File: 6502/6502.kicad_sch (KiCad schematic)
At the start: 34 parts, among them SW1 SW_Push, SW2 SW_Push, U1 74LS08, U10 NHD-0420H1Z, U12 65C02S, U2 ATF22V10C, U3 74LS154, U4 AS6C4008-55PCN, U5 28C256, U7 6522, U8 6522, X1 ACO-4MHz

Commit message: pcb almost done
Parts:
- C6: renamed from C15; footprint Capacitor_THT:C_Radial_D8.0mm_H7.0mm_P3.50mm -> Capacitor_THT:C_Radial_D10.0mm_H20.0mm_P5.00mm
- renumbered C8 to C10, C9 to C11, C6 to C7, C16 to C8, C7 to C9, R7 to R1, R5 to R2, R2 to R3, R8 to R5, R1 to R6, R9 to R7, R6 to R8, R3 to R9, SW2 to SW1, SW1 to SW2, U3 to U2, U5 to U3, U2 to U4, U12 to U5, U4 to U6, U10 to U9
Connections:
- net EXT_IN2: no longer U2.18 (E0), U4.3 (I1), U5.25 (A15)
- new net a15: U2.18 (E0), U4.3 (I1), U5.25 (A15)

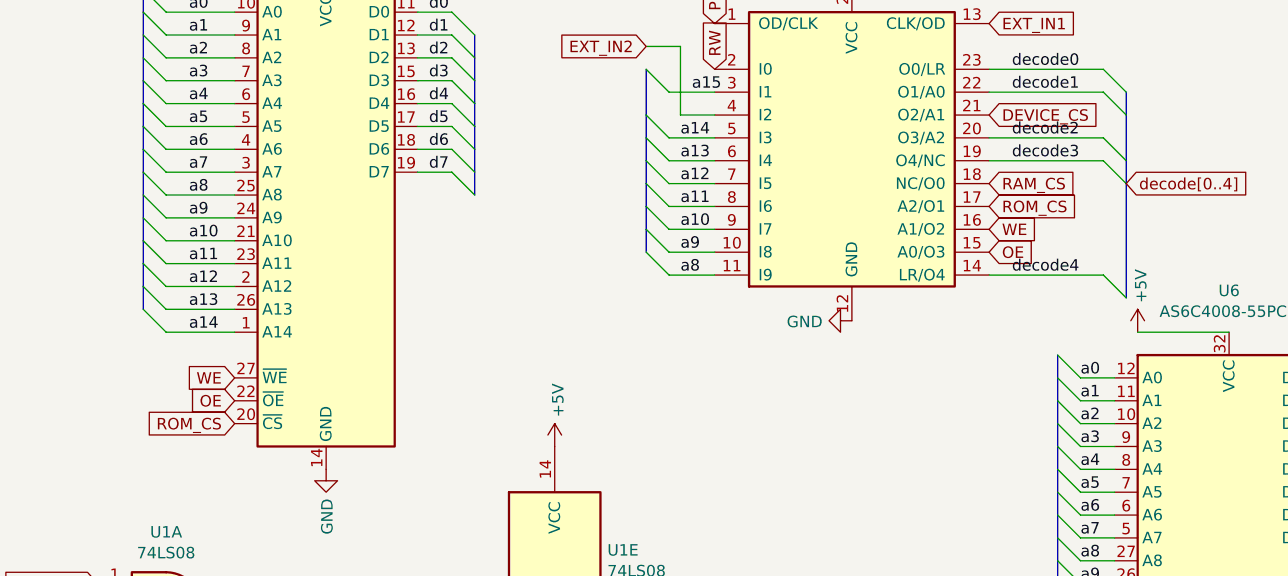
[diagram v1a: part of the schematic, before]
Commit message: fixed decoder circuit
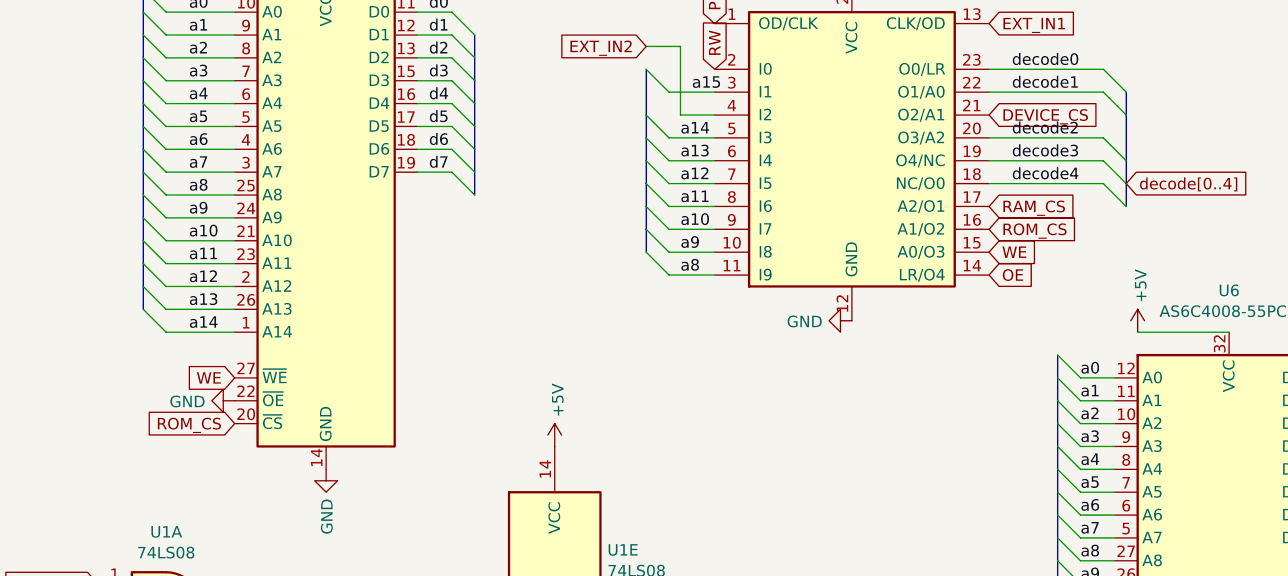
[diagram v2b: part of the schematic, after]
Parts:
- RV1: footprint 6502Computer:10 kOhms 12 Watt Square Cermet Potentiometer -> Potentiometer_THT:Potentiometer_Bourns_3266W_Vertical
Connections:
- net GND: now also U3.22 (~{OE})
- net OE: now also U4.14 (LR/O4); no longer U3.22 (~{OE}), U4.15 (A0/O3)
- net RAM_CS: now also U4.17 (A2/O1); no longer U4.18 (NC/O0)
- net ROM_CS: now also U4.16 (A1/O2); no longer U4.17 (A2/O1)
- net WE: now also U4.15 (A0/O3); no longer U4.16 (A1/O2)
- net decode4: now also U4.18 (NC/O0); no longer U4.14 (LR/O4)

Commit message: updated pcb
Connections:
- net decode3 is gone; now on net VIA2_CS: U4.19 (O4/NC)
- net decode4 is gone; now on net VIA1_CS: U4.18 (NC/O0)
- net VIA1_CS: no longer U2.1 (S0)
- net VIA2_CS: no longer U2.2 (S1)
- net EXT_IN1: no longer names the net of U4.13 (CLK/OD)
- net EXT_IN2: no longer names the net of U4.4 (I2)
- net PHI1O: no longer names the net of U5.3 (PHI1O)
- net dev10 renamed IO10
- net dev11 renamed IO11
- net dev12 renamed IO12
- net dev13 renamed IO13
- net dev14 renamed IO14
- net dev15 renamed IO15
- net dev2 renamed IO2
- net dev3 renamed IO3
- net dev4 renamed IO4
- net dev5 renamed IO5
- net dev6 renamed IO6
- net dev7 renamed IO7
- net dev8 renamed IO8
- net dev9 renamed IO9
- new net IO0: U2.1 (S0)
- new net IO1: U2.2 (S1)
- no-connect marks 1 -> 4

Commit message: changes
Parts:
- added R10: 220Ω, Resistor_THT:R_Axial_DIN0207_L6.3mm_D2.5mm_P10.16mm_Horizontal, symbol Device:R
- R1, R2, R3, R4, R5, R6, R7, R8: footprint Resistor_THT:R_Axial_DIN0207_L6.3mm_D2.5mm_P7.62mm_Horizontal -> Resistor_THT:R_Axial_DIN0204_L3.6mm_D1.6mm_P7.62mm_Horizontal
- R9: footprint Resistor_THT:R_Axial_DIN0207_L6.3mm_D2.5mm_P7.62mm_Horizontal -> Resistor_THT:R_Axial_DIN0207_L6.3mm_D2.5mm_P10.16mm_Horizontal
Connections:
- net GND: now also R10.1; no longer SW1.1
- new net: R10.2, SW1.1
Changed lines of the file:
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@@
       (effects (font (size 1.27 1.27)) (justify left))
     )
-    (property "Footprint" "Resistor_THT:R_Axial_DIN0207_L6.3mm_D2.5mm_P7.62mm_Horizontal" (id 2) (at 131.572 25.4 90)
+    (property "Footprint" "Resistor_THT:R_Axial_DIN0204_L3.6mm_D1.6mm_P7.62mm_Horizontal" (id 2) (at 131.572 25.4 90)
       (effects (font (size 1.27 1.27)) hide)
     )
@@
     (property "Reference" "R9" (id 0) (at 238.76 17.6022 90))
     (property "Value" "220Ω" (id 1) (at 238.76 19.9136 90))
-    (property "Footprint" "Resistor_THT:R_Axial_DIN0207_L6.3mm_D2.5mm_P7.62mm_Horizontal" (id 2) (at 238.76 21.082 90)
+    (property "Footprint" "Resistor_THT:R_Axial_DIN0207_L6.3mm_D2.5mm_P10.16mm_Horizontal" (id 2) (at 238.76 21.082 90)
       (effects (font (size 1.27 1.27)) hide)
     )
@@
       (effects (font (size 1.27 1.27)) (justify left))
     )
-    (property "Footprint" "Resistor_THT:R_Axial_DIN0207_L6.3mm_D2.5mm_P7.62mm_Horizontal" (id 2) (at 96.012 25.4 90)
+    (property "Footprint" "Resistor_THT:R_Axial_DIN0204_L3.6mm_D1.6mm_P7.62mm_Horizontal" (id 2) (at 96.012 25.4 90)
       (effects (font (size 1.27 1.27)) hide)
     )
@@
     (pin "2")
   )
-  (symbol (lib_id "power:GND") (at 76.2 41.91 0) (unit 1)
-    (in_bom yes) (on_board yes)
-    (property "Reference" "#PWR012" (id 0) (at 76.2 48.26 0)
-      (effects (font (size 1.27 1.27)) hide)
-    )
-    (property "Value" "GND" (id 1) (at 76.327 45.1612 90)
+  (symbol (lib_id "power:GND") (at 76.2 49.53 0) (unit 1)
+    (in_bom yes) (on_board yes)
+    (property "Reference" "#PWR012" (id 0) (at 76.2 55.88 0)
+      (effects (font (size 1.27 1.27)) hide)
+    )
+    (property "Value" "GND" (id 1) (at 76.327 52.7812 90)
       (effects (font (size 1.27 1.27)) (justify right))
     )
-    (property "Footprint" "" (id 2) (at 76.2 41.91 0)
-      (effects (font (size 1.27 1.27)) hide)
-    )
-    (property "Datasheet" "" (id 3) (at 76.2 41.91 0)
+    (property "Footprint" "" (id 2) (at 76.2 49.53 0)
+      (effects (font (size 1.27 1.27)) hide)
+    )
+    (property "Datasheet" "" (id 3) (at 76.2 49.53 0)
       (effects (font (size 1.27 1.27)) hide)
     )
@@
       (effects (font (size 1.27 1.27)) (justify left))
     )
-    (property "Footprint" "Resistor_THT:R_Axial_DIN0207_L6.3mm_D2.5mm_P7.62mm_Horizontal" (id 2) (at 84.582 38.1 90)
+    (property "Footprint" "Resistor_THT:R_Axial_DIN0204_L3.6mm_D1.6mm_P7.62mm_Horizontal" (id 2) (at 84.582 38.1 90)
       (effects (font (size 1.27 1.27)) hide)
     )
@@
       (effects (font (size 1.27 1.27)) (justify left))
     )
-    (property "Footprint" "Resistor_THT:R_Axial_DIN0207_L6.3mm_D2.5mm_P7.62mm_Horizontal" (id 2) (at 146.812 43.18 90)
+    (property "Footprint" "Resistor_THT:R_Axial_DIN0204_L3.6mm_D1.6mm_P7.62mm_Horizontal" (id 2) (at 146.812 43.18 90)
       (effects (font (size 1.27 1.27)) hide)
     )
@@
       (effects (font (size 1.27 1.27)) (justify left))
     )
-    (property "Footprint" "Resistor_THT:R_Axial_DIN0207_L6.3mm_D2.5mm_P7.62mm_Horizontal" (id 2) (at 121.412 186.69 90)
+    (property "Footprint" "Resistor_THT:R_Axial_DIN0204_L3.6mm_D1.6mm_P7.62mm_Horizontal" (id 2) (at 121.412 186.69 90)
       (effects (font (size 1.27 1.27)) hide)
     )
@@
       (effects (font (size 1.27 1.27)) (justify left))
     )
-    (property "Footprint" "Resistor_THT:R_Axial_DIN0207_L6.3mm_D2.5mm_P7.62mm_Horizontal" (id 2) (at 115.062 186.69 90)
+    (property "Footprint" "Resistor_THT:R_Axial_DIN0204_L3.6mm_D1.6mm_P7.62mm_Horizontal" (id 2) (at 115.062 186.69 90)
       (effects (font (size 1.27 1.27)) hide)
     )
@@
       (effects (font (size 1.27 1.27)) (justify left))
     )
-    (property "Footprint" "Resistor_THT:R_Axial_DIN0207_L6.3mm_D2.5mm_P7.62mm_Horizontal" (id 2) (at 126.492 186.69 90)
+    (property "Footprint" "Resistor_THT:R_Axial_DIN0204_L3.6mm_D1.6mm_P7.62mm_Horizontal" (id 2) (at 126.492 186.69 90)
       (effects (font (size 1.27 1.27)) hide)
     )
@@
       (effects (font (size 1.27 1.27)) (justify left))
     )
-    (property "Footprint" "Resistor_THT:R_Axial_DIN0207_L6.3mm_D2.5mm_P7.62mm_Horizontal" (id 2) (at 132.842 186.69 90)
+    (property "Footprint" "Resistor_THT:R_Axial_DIN0204_L3.6mm_D1.6mm_P7.62mm_Horizontal" (id 2) (at 132.842 186.69 90)
       (effects (font (size 1.27 1.27)) hide)
     )
@@
     (pin "1")
   )
+  (symbol (lib_id "Device:R") (at 76.2 45.72 180) (unit 1)
+    (in_bom yes) (on_board yes)
+    (property "Reference" "R10" (id 0) (at 79.375 44.45 0))
+    (property "Value" "220Ω" (id 1) (at 80.01 46.355 0))
+    (property "Footprint" "Resistor_THT:R_Axial_DIN0207_L6.3mm_D2.5mm_P10.16mm_Horizontal" (id 2) (at 77.978 45.72 90)
+      (effects (font (size 1.27 1.27)) hide)
+    )
+    (property "Datasheet" "~" (id 3) (at 76.2 45.72 0)
+      (effects (font (size 1.27 1.27)) hide)
+    )
+    (pin "1")
+    (pin "2")
+  )
   (sheet (at 17.78 168.91) (size 27.94 3.81) (fields_autoplaced)
     (stroke (width 0) (type solid) (color 0 0 0 0))
@@
     )
     (path "/00000000-0000-0000-0000-000062fb2665"
-      (reference "R1") (unit 1) (value "10K") (footprint "Resistor_THT:R_Axial_DIN0207_L6.3mm_D2.5mm_P7.62mm_Horizontal")
+      (reference "R1") (unit 1) (value "10K") (footprint "Resistor_THT:R_Axial_DIN0204_L3.6mm_D1.6mm_P7.62mm_Horizontal")
     )
     (path "/00000000-0000-0000-0000-000062f715c5"
-      (reference "R2") (unit 1) (value "1K") (footprint "Resistor_THT:R_Axial_DIN0207_L6.3mm_D2.5mm_P7.62mm_Horizontal")
+      (reference "R2") (unit 1) (value "1K") (footprint "Resistor_THT:R_Axial_DIN0204_L3.6mm_D1.6mm_P7.62mm_Horizontal")
     )
     (path "/00000000-0000-0000-0000-0000630bfb62"
-      (reference "R3") (unit 1) (value "1K") (footprint "Resistor_THT:R_Axial_DIN0207_L6.3mm_D2.5mm_P7.62mm_Horizontal")
+      (reference "R3") (unit 1) (value "1K") (footprint "Resistor_THT:R_Axial_DIN0204_L3.6mm_D1.6mm_P7.62mm_Horizontal")
     )
     (path "/00000000-0000-0000-0000-0000630beb07"
-      (reference "R4") (unit 1) (value "1K") (footprint "Resistor_THT:R_Axial_DIN0207_L6.3mm_D2.5mm_P7.62mm_Horizontal")
+      (reference "R4") (unit 1) (value "1K") (footprint "Resistor_THT:R_Axial_DIN0204_L3.6mm_D1.6mm_P7.62mm_Horizontal")
     )
     (path "/00000000-0000-0000-0000-0000630c061b"
-      (reference "R5") (unit 1) (value "1K") (footprint "Resistor_THT:R_Axial_DIN0207_L6.3mm_D2.5mm_P7.62mm_Horizontal")
+      (reference "R5") (unit 1) (value "1K") (footprint "Resistor_THT:R_Axial_DIN0204_L3.6mm_D1.6mm_P7.62mm_Horizontal")
     )
     (path "/00000000-0000-0000-0000-00006230e643"
-      (reference "R6") (unit 1) (value "1K") (footprint "Resistor_THT:R_Axial_DIN0207_L6.3mm_D2.5mm_P7.62mm_Horizontal")
+      (reference "R6") (unit 1) (value "1K") (footprint "Resistor_THT:R_Axial_DIN0204_L3.6mm_D1.6mm_P7.62mm_Horizontal")
     )
     (path "/00000000-0000-0000-0000-0000630e41f6"
-      (reference "R7") (unit 1) (value "1K") (footprint "Resistor_THT:R_Axial_DIN0207_L6.3mm_D2.5mm_P7.62mm_Horizontal")
+      (reference "R7") (unit 1) (value "1K") (footprint "Resistor_THT:R_Axial_DIN0204_L3.6mm_D1.6mm_P7.62mm_Horizontal")
     )
     (path "/00000000-0000-0000-0000-000063003a9a"
-      (reference "R8") (unit 1) (value "1K") (footprint "Resistor_THT:R_Axial_DIN0207_L6.3mm_D2.5mm_P7.62mm_Horizontal")
+      (reference "R8") (unit 1) (value "1K") (footprint "Resistor_THT:R_Axial_DIN0204_L3.6mm_D1.6mm_P7.62mm_Horizontal")
     )
     (path "/00000000-0000-0000-0000-0000624aefc0"
-      (reference "R9") (unit 1) (value "220Ω") (footprint "Resistor_THT:R_Axial_DIN0207_L6.3mm_D2.5mm_P7.62mm_Horizontal")
+      (reference "R9") (unit 1) (value "220Ω") (footprint "Resistor_THT:R_Axial_DIN0207_L6.3mm_D2.5mm_P10.16mm_Horizontal")
+    )
+    (path "/fa2fd8ac-9eaa-4c1b-bfce-279247c19abe"
+      (reference "R10") (unit 1) (value "220Ω") (footprint "Resistor_THT:R_Axial_DIN0207_L6.3mm_D2.5mm_P10.16mm_Horizontal")
     )
     (path "/00000000-0000-0000-0000-0000623fdcfb"
